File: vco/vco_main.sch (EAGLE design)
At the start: 101 parts, among them IC1 OPA4130U, IC2 LM13700M, IC3 OPA4130U, IC4 OPA4130U, Q1 MMBFJ3

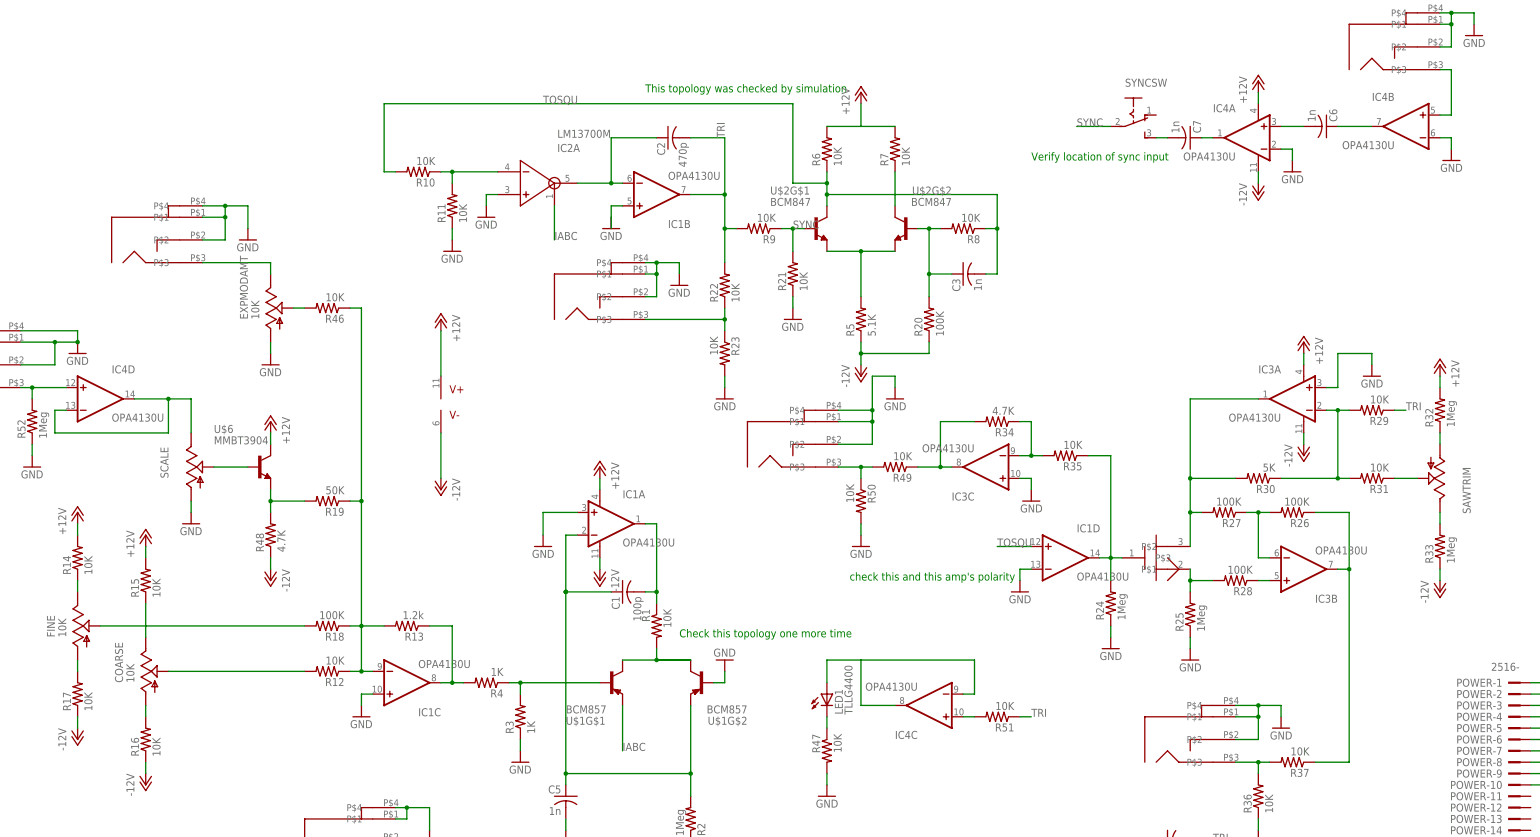
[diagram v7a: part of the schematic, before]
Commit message: cleaned up the layout a bit.  fixed component values.
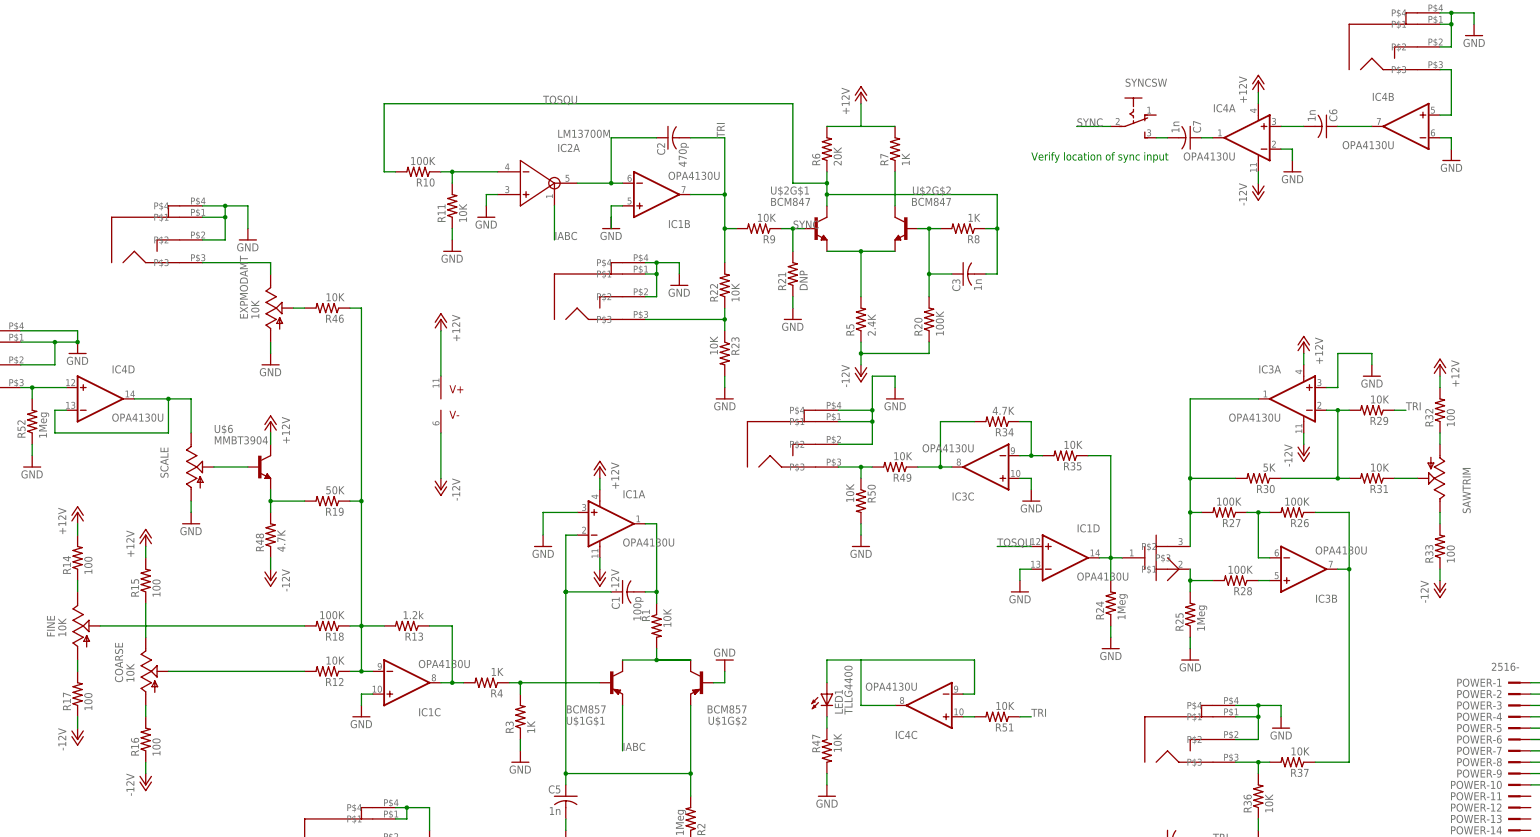
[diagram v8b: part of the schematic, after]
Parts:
- R10: value 10K -> 100K
- R14, R15, R16, R17: value 10K -> 100
- R21: value 10K -> DNP
- R32, R33: value 1Meg -> 100
- R5: value 5.1K -> 2.4K
- R6: value 10K -> 20K
- R7, R8: value 10K -> 1K
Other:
- note removed: "Check this topology one more time"
- note removed: "This topology was checked by simulation"
- note removed: "check this and this amp's polarity"
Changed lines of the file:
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@@
 <part name="GND3" library="dan" deviceset="GND" device=""/>
 <part name="U$2" library="dan" deviceset="BCM847" device=""/>
-<part name="R5" library="dan" deviceset="R-US_" device="R0603" value="5.1K"/>
-<part name="R6" library="dan" deviceset="R-US_" device="R0603" value="10K"/>
-<part name="R7" library="dan" deviceset="R-US_" device="R0603" value="10K"/>
+<part name="R5" library="dan" deviceset="R-US_" device="R0603" value="2.4K"/>
+<part name="R6" library="dan" deviceset="R-US_" device="R0603" value="20K"/>
+<part name="R7" library="dan" deviceset="R-US_" device="R0603" value="1K"/>
 <part name="P+3" library="dan" deviceset="+12V" device=""/>
 <part name="P-2" library="dan" deviceset="-12V" device=""/>
-<part name="R8" library="dan" deviceset="R-US_" device="R0603" value="10K"/>
+<part name="R8" library="dan" deviceset="R-US_" device="R0603" value="1K"/>
 <part name="R9" library="dan" deviceset="R-US_" device="R0603" value="10K"/>
-<part name="R10" library="dan" deviceset="R-US_" device="R0603" value="10K"/>
+<part name="R10" library="dan" deviceset="R-US_" device="R0603" value="100K"/>
 <part name="R11" library="dan" deviceset="R-US_" device="R0603" value="10K"/>
 <part name="GND4" library="dan" deviceset="GND" device=""/>
@@
 <part name="GND6" library="dan" deviceset="GND" device=""/>
 <part name="COARSE" library="dan" deviceset="US-EVU" device="F2J" value="10K"/>
-<part name="R15" library="dan" deviceset="R-US_" device="R0603" value="10K"/>
-<part name="R16" library="dan" deviceset="R-US_" device="R0603" value="10K"/>
+<part name="R15" library="dan" deviceset="R-US_" device="R0603" value="100"/>
+<part name="R16" library="dan" deviceset="R-US_" device="R0603" value="100"/>
 <part name="P-3" library="dan" deviceset="-12V" device=""/>
 <part name="P+4" library="dan" deviceset="+12V" device=""/>
@@
 <part name="C1" library="dan" deviceset="C-US" device="C0603" value="100p"/>
 <part name="FINE" library="dan" deviceset="US-EVU" device="F2J" value="10K"/>
-<part name="R14" library="dan" deviceset="R-US_" device="R0603" value="10K"/>
-<part name="R17" library="dan" deviceset="R-US_" device="R0603" value="10K"/>
+<part name="R14" library="dan" deviceset="R-US_" device="R0603" value="100"/>
+<part name="R17" library="dan" deviceset="R-US_" device="R0603" value="100"/>
 <part name="P-4" library="dan" deviceset="-12V" device=""/>
 <part name="P+2" library="dan" deviceset="+12V" device=""/>
@@
 <part name="R20" library="dan" deviceset="R-US_" device="R0603" value="100K"/>
 <part name="C3" library="dan" deviceset="C-US" device="C0603" value="1n"/>
-<part name="R21" library="dan" deviceset="R-US_" device="R0603" value="10K"/>
+<part name="R21" library="dan" deviceset="R-US_" device="R0603" value="DNP"/>
 <part name="GND10" library="dan" deviceset="GND" device=""/>
 <part name="TRIOUT" library="dan" deviceset="PJ301BM" device=""/>
@@
 <part name="R31" library="dan" deviceset="R-US_" device="R0603" value="10K"/>
 <part name="SAWTRIM" library="dan" deviceset="TRIM_US-" device="B64Y"/>
-<part name="R32" library="dan" deviceset="R-US_" device="R0603" value="1Meg"/>
-<part name="R33" library="dan" deviceset="R-US_" device="R0603" value="1Meg"/>
+<part name="R32" library="dan" deviceset="R-US_" device="R0603" value="100"/>
+<part name="R33" library="dan" deviceset="R-US_" device="R0603" value="100"/>
 <part name="P+6" library="dan" deviceset="+12V" device=""/>
 <part name="P-7" library="dan" deviceset="-12V" device=""/>
@@
 <sheet>
 <plain>
-<text x="124.46" y="38.1" size="1.778" layer="91">check this and this amp's polarity</text>
-<text x="78.74" y="147.32" size="1.778" layer="91">This topology was checked by simulation</text>
-<text x="86.36" y="25.4" size="1.778" layer="91">Check this topology one more time</text>
 <text x="165.1" y="132.08" size="1.778" layer="91">Verify location of sync input</text>
 </plain>
